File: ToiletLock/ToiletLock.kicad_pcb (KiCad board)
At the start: 2 copper layers, 27 parts, among them J1 Conn_01x02_Male, U1 DRV8837C, U2 APDS-9960, Y1 Crystal_GND24

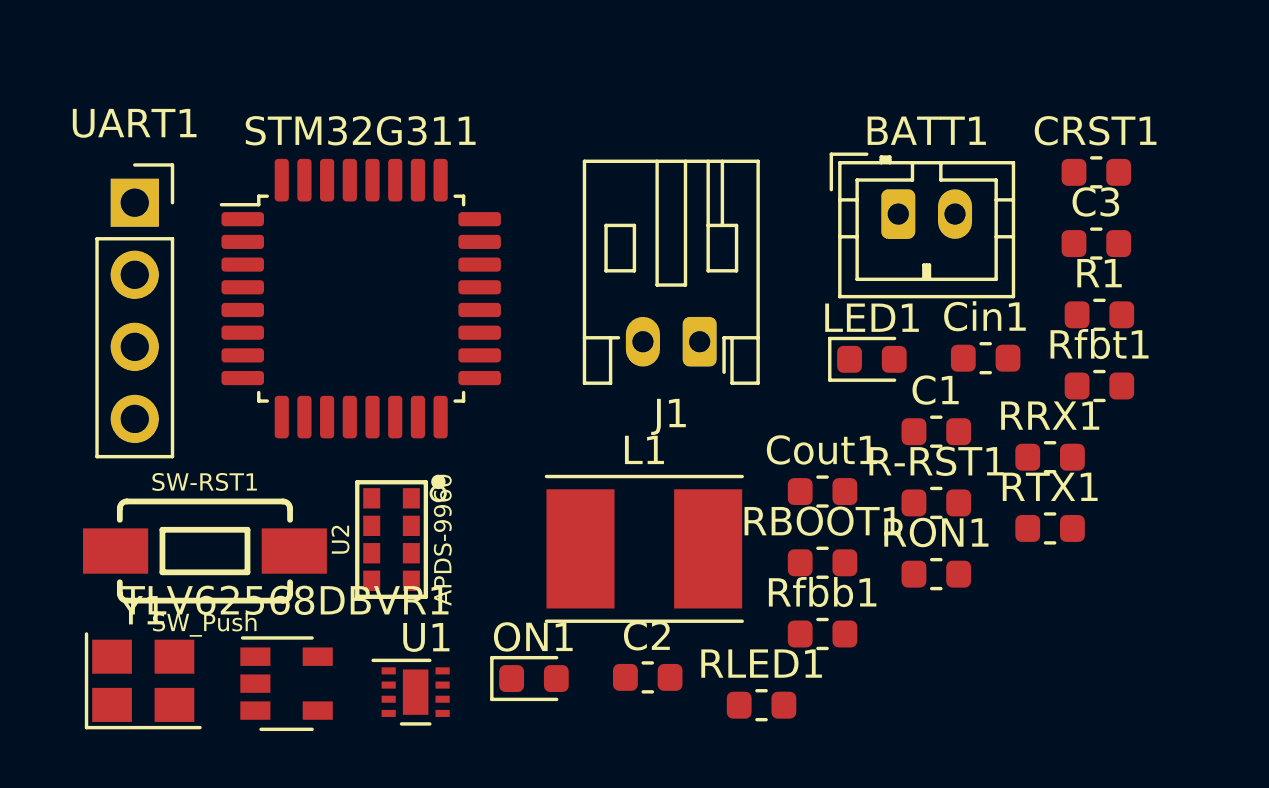
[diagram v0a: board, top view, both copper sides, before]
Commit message: del useless file
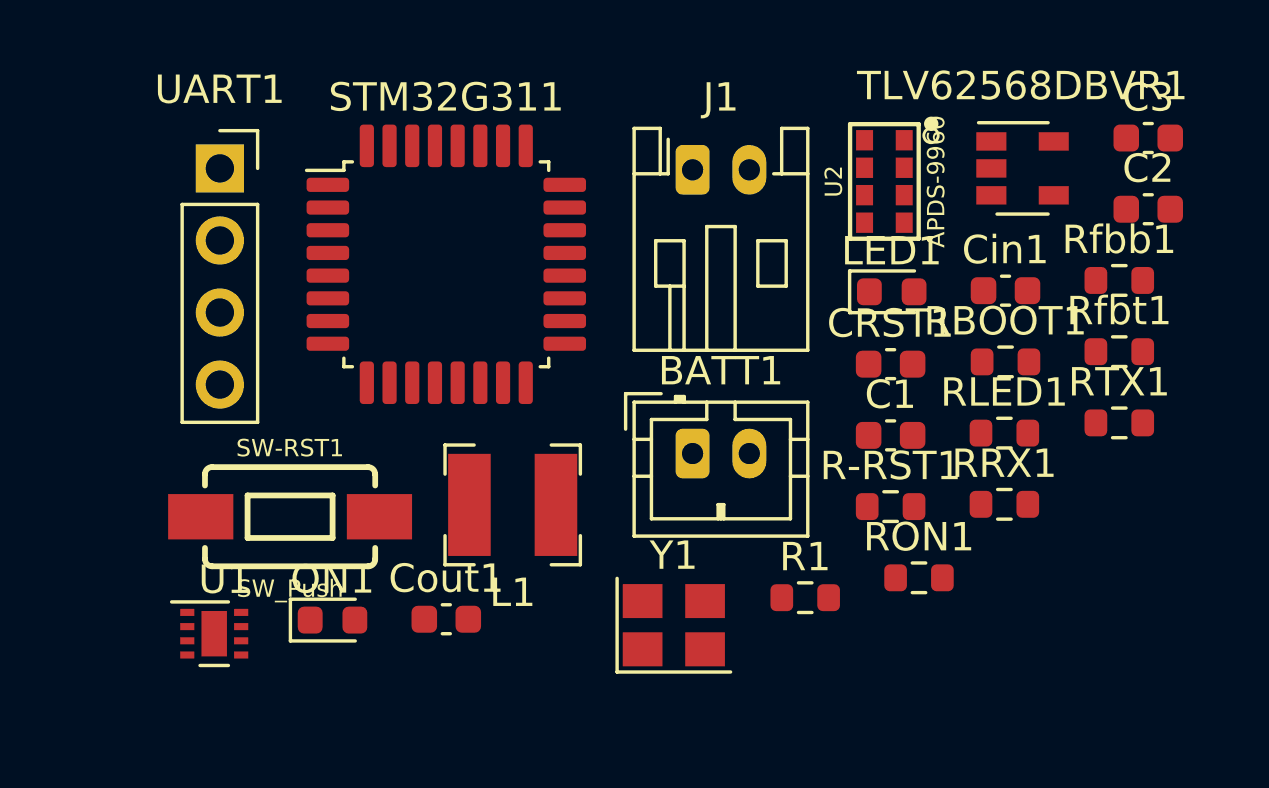
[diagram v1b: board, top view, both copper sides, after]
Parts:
- L1: footprint Inductor_SMD:L_Taiyo-Yuden_NR-50xx_HandSoldering -> Inductor_SMD:L_Bourns-SRN4018
- moved TLV62568DBVR1 31.7 mm to (138.6, 81.4)
- moved C2 24.2 mm to (143.1, 82.8)
- moved U2 21.5 mm to (133.8, 81.9)
- moved Y1 18.8 mm to (126.3, 97.5)
- moved Rfbb1 16.3 mm to (142.0, 85.3)
- moved R1 14.4 mm to (131.0, 96.5)
- moved Cout1 14.0 mm to (118.3, 97.3)
- moved RLED1 12.9 mm to (138.0, 90.7)
- moved BATT1 11.1 mm to (127.0, 91.4)
- moved CRST1 9.91 mm to (134.0, 88.3)
- moved RBOOT1 9.58 mm to (138.0, 88.2)
- moved ON1 7.39 mm to (114.3, 97.3)
- moved U1 7.39 mm to (110.1, 97.8)
- moved J1 6.07 mm to (127.0, 81.4), turned to 0 degrees
- moved L1 4.89 mm to (120.7, 93.2)
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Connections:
- STM32G311 pad 10: (no net) -> Net-(STM32G311-Pad10)
- STM32G311 pad 11: (no net) -> Net-(STM32G311-Pad11)
- STM32G311 pad 12: (no net) -> Net-(STM32G311-Pad12)
- STM32G311 pad 13: (no net) -> Net-(STM32G311-Pad13)
- STM32G311 pad 14: (no net) -> Net-(STM32G311-Pad14)
- STM32G311 pad 15: (no net) -> Net-(STM32G311-Pad15)
- STM32G311 pad 16: (no net) -> Net-(STM32G311-Pad16)
- STM32G311 pad 17: (no net) -> Net-(STM32G311-Pad17)
- STM32G311 pad 18: (no net) -> Net-(STM32G311-Pad18)
- STM32G311 pad 22: (no net) -> Net-(STM32G311-Pad22)
- STM32G311 pad 23: (no net) -> Net-(STM32G311-Pad23)
- STM32G311 pad 24: (no net) -> /SWDIO
- STM32G311 pad 26: (no net) -> /USART2-RX
- STM32G311 pad 27: (no net) -> Net-(STM32G311-Pad27)
- STM32G311 pad 28: (no net) -> Net-(STM32G311-Pad28)
- STM32G311 pad 29: (no net) -> Net-(STM32G311-Pad29)
- STM32G311 pad 30: (no net) -> Net-(STM32G311-Pad30)
- STM32G311 pad 7: (no net) -> Net-(STM32G311-Pad7)
- STM32G311 pad 8: (no net) -> Net-(STM32G311-Pad8)
- STM32G311 pad 9: (no net) -> Net-(STM32G311-Pad9)
- U1 pad 4: Net-(U1-Pad4) -> GND
- U1 pad 5: (no net) -> /M2
- U1 pad 6: (no net) -> /M1
- U1 pad 7: (no net) -> /SLEEP
- U1 pad 9: Net-(U1-Pad4) -> GND
- U2 pad 2: (no net) -> /INT
